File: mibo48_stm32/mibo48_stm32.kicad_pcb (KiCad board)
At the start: 2 copper layers, 55.9 x 20.3 mm, 33 parts, among them J1 Conn_01x02, J2 Conn_01x22, J3 Conn_01x22, J4 USB_B_Micro, J5 Conn_01x04, SW1 Reset, U1 STM32F303CBTx, U2 AMS1117-3.3, Y1 8MHz, Y2 32.768kHz

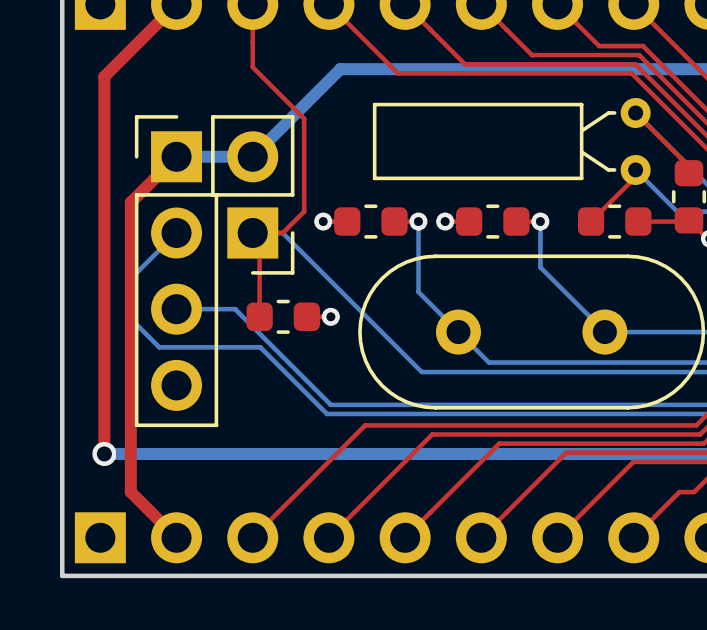
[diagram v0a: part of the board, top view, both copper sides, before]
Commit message: small layout change
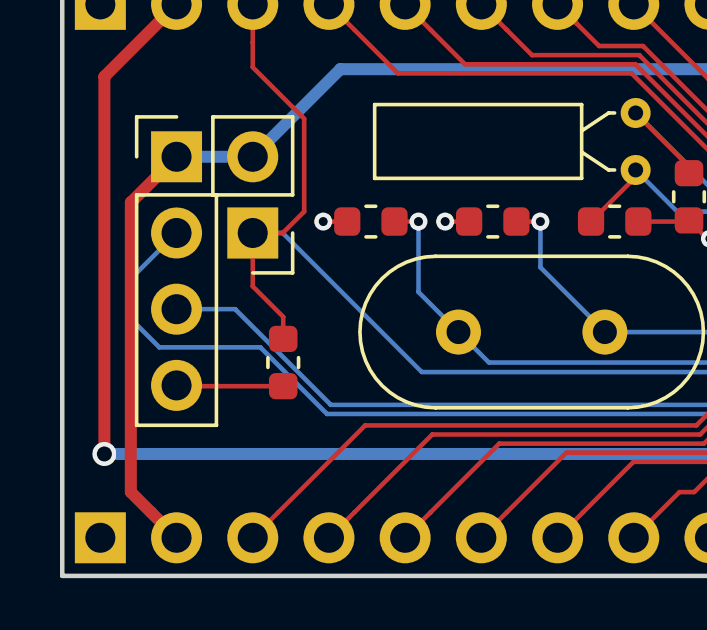
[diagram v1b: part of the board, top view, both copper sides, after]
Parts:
- moved R1 1.52 mm to (135.6, 108.5), turned to 270 degrees
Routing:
- net GND: track 33.7 -> 36.4 mm, vias 15 -> 14
- net /BOOT0: track 43.0 -> 44.0 mm
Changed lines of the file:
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@@
     (thickness 1.6)
     (drawings 7)
-    (tracks 474)
+    (tracks 475)
     (zones 0)
     (modules 33)
@@
     (45 Margin user)
     (46 B.CrtYd user hide)
-    (47 F.CrtYd user hide)
+    (47 F.CrtYd user)
     (48 B.Fab user)
     (49 F.Fab user hide)
@@
     (add_net /5V)
   )
+  (module Resistor_SMD:R_0603_1608Metric (layer F.Cu)
+    (at 135.636 108.458 270)
+    (descr "Resistor SMD 0603 (1608 Metric), square (rectangular) end terminal, IPC_7351 nominal, (Body size source: http://www.tortai-tech.com/upload/download/2011102023233369053.pdf), generated with kicad-footprint-generator")
+    (tags resistor)
+    (attr smd)
+    (fp_text reference R1 (at 0 -1.43 270) (layer F.SilkS) hide
+      (effects (font (size 1 1) (thickness 0.15)))
+    )
+    (fp_text value 100k (at 0 1.43 270) (layer F.Fab)
+      (effects (font (size 1 1) (thickness 0.15)))
+    )
+    (fp_line (start -0.8 0.4) (end -0.8 -0.4) (layer F.Fab) (width 0.1))
+    (fp_line (start -0.8 -0.4) (end 0.8 -0.4) (layer F.Fab) (width 0.1))
+    (fp_line (start 0.8 -0.4) (end 0.8 0.4) (layer F.Fab) (width 0.1))
+    (fp_line (start 0.8 0.4) (end -0.8 0.4) (layer F.Fab) (width 0.1))
+    (fp_line (start -0.162779 -0.51) (end 0.162779 -0.51) (layer F.SilkS) (width 0.12))
+    (fp_line (start -0.162779 0.51) (end 0.162779 0.51) (layer F.SilkS) (width 0.12))
+    (fp_line (start -1.48 0.73) (end -1.48 -0.73) (layer F.CrtYd) (width 0.05))
+    (fp_line (start -1.48 -0.73) (end 1.48 -0.73) (layer F.CrtYd) (width 0.05))
+    (fp_line (start 1.48 -0.73) (end 1.48 0.73) (layer F.CrtYd) (width 0.05))
+    (fp_line (start 1.48 0.73) (end -1.48 0.73) (layer F.CrtYd) (width 0.05))
+    (fp_text user %R (at 0 0 270) (layer F.Fab)
+      (effects (font (size 0.4 0.4) (thickness 0.06)))
+    )
+    (pad 1 smd roundrect (at -0.7875 0 270) (size 0.875 0.95) (layers F.Cu F.Paste F.Mask) (roundrect_rratio 0.25)
+      (net 8 /BOOT0))
+    (pad 2 smd roundrect (at 0.7875 0 270) (size 0.875 0.95) (layers F.Cu F.Paste F.Mask) (roundrect_rratio 0.25)
+      (net 1 GND))
+    (model ${KISYS3DMOD}/Resistor_SMD.3dshapes/R_0603_1608Metric.wrl
+      (at (xyz 0 0 0))
+      (scale (xyz 1 1 1))
+      (rotate (xyz 0 0 0))
+    )
+  )
   (module Button_Switch_SMD:SW_SPST_CK_RS282G05A3 (layer F.Cu)
     (at 172.974 101.219)
@@
       (net 1 GND))
     (model ${KISYS3DMOD}/Connector_PinHeader_2.54mm.3dshapes/PinHeader_1x04_P2.54mm_Vertical.wrl
-      (at (xyz 0 0 0))
-      (scale (xyz 1 1 1))
-      (rotate (xyz 0 0 0))
-    )
-  )
-  (module Resistor_SMD:R_0603_1608Metric (layer F.Cu)
-    (at 135.636 106.934)
-    (descr "Resistor SMD 0603 (1608 Metric), square (rectangular) end terminal, IPC_7351 nominal, (Body size source: http://www.tortai-tech.com/upload/download/2011102023233369053.pdf), generated with kicad-footprint-generator")
-    (tags resistor)
-    (attr smd)
-    (fp_text reference R1 (at 0 -1.43) (layer F.SilkS) hide
-      (effects (font (size 1 1) (thickness 0.15)))
-    )
-    (fp_text value 100k (at 0 1.43) (layer F.Fab)
-      (effects (font (size 1 1) (thickness 0.15)))
-    )
-    (fp_line (start -0.8 0.4) (end -0.8 -0.4) (layer F.Fab) (width 0.1))
-    (fp_line (start -0.8 -0.4) (end 0.8 -0.4) (layer F.Fab) (width 0.1))
-    (fp_line (start 0.8 -0.4) (end 0.8 0.4) (layer F.Fab) (width 0.1))
-    (fp_line (start 0.8 0.4) (end -0.8 0.4) (layer F.Fab) (width 0.1))
-    (fp_line (start -0.162779 -0.51) (end 0.162779 -0.51) (layer F.SilkS) (width 0.12))
-    (fp_line (start -0.162779 0.51) (end 0.162779 0.51) (layer F.SilkS) (width 0.12))
-    (fp_line (start -1.48 0.73) (end -1.48 -0.73) (layer F.CrtYd) (width 0.05))
-    (fp_line (start -1.48 -0.73) (end 1.48 -0.73) (layer F.CrtYd) (width 0.05))
-    (fp_line (start 1.48 -0.73) (end 1.48 0.73) (layer F.CrtYd) (width 0.05))
-    (fp_line (start 1.48 0.73) (end -1.48 0.73) (layer F.CrtYd) (width 0.05))
-    (fp_text user %R (at 0 0) (layer F.Fab)
-      (effects (font (size 0.4 0.4) (thickness 0.06)))
-    )
-    (pad 1 smd roundrect (at -0.7875 0) (size 0.875 0.95) (layers F.Cu F.Paste F.Mask) (roundrect_rratio 0.25)
-      (net 8 /BOOT0))
-    (pad 2 smd roundrect (at 0.7875 0) (size 0.875 0.95) (layers F.Cu F.Paste F.Mask) (roundrect_rratio 0.25)
-      (net 1 GND))
-    (model ${KISYS3DMOD}/Resistor_SMD.3dshapes/R_0603_1608Metric.wrl
       (at (xyz 0 0 0))
       (scale (xyz 1 1 1))
@@
   (via (at 136.9695 103.759) (size 0.6) (drill 0.3) (layers F.Cu B.Cu) (net 1))
   (segment (start 137.7695 103.759) (end 136.9695 103.759) (width 0.152) (layer F.Cu) (net 1))
-  (via (at 137.2235 106.934) (size 0.6) (drill 0.3) (layers F.Cu B.Cu) (net 1))
-  (segment (start 136.4235 106.934) (end 137.2235 106.934) (width 0.152) (layer F.Cu) (net 1))
   (segment (start 153.725112 110.917388) (end 153.2635 111.379) (width 0.152) (layer F.Cu) (net 1))
   (segment (start 154.236686 110.675994) (end 154.236125 110.676555) (width 0.152) (layer F.Cu) (net 1))
@@
   (segment (start 154.755435 103.492096) (end 154.755435 103.761538) (width 0.152) (layer F.Cu) (net 1))
   (segment (start 154.127755 102.864416) (end 154.755435 103.492096) (width 0.152) (layer F.Cu) (net 1))
+  (segment (start 132.1055 109.2455) (end 132.08 109.22) (width 0.152) (layer F.Cu) (net 1))
+  (segment (start 135.636 109.2455) (end 132.1055 109.2455) (width 0.152) (layer F.Cu) (net 1))
   (via (at 140.1445 103.759) (size 0.6) (drill 0.3) (layers F.Cu B.Cu) (net 2))
   (segment (start 139.3445 103.759) (end 140.1445 103.759) (width 0.152) (layer F.Cu) (net 2))
@@
   (segment (start 172.314 107.95) (end 171.7675 107.95) (width 0.4) (layer F.Cu) (net 5))
   (segment (start 171.7675 107.95) (end 169.291 105.4735) (width 0.4) (layer F.Cu) (net 5))
-  (via (at 159.7025 98.933) (size 0.6) (drill 0.3) (layers F.Cu B.Cu) (net 5) (status 1000000))
-  (segment (start 160.5025 99.314) (end 160.040888 98.852388) (width 0.4) (layer F.Cu) (net 5) (status 1000000))
-  (segment (start 159.783112 98.852388) (end 159.7025 98.933) (width 0.4) (layer F.Cu) (net 5) (status 1000000))
-  (segment (start 160.040888 98.852388) (end 159.783112 98.852388) (width 0.4) (layer F.Cu) (net 5) (status 1000000))
+  (via (at 159.7025 98.933) (size 0.6) (drill 0.3) (layers F.Cu B.Cu) (net 5))
+  (segment (start 160.5025 99.314) (end 160.040888 98.852388) (width 0.4) (layer F.Cu) (net 5))
+  (segment (start 159.783112 98.852388) (end 159.7025 98.933) (width 0.4) (layer F.Cu) (net 5))
+  (segment (start 160.040888 98.852388) (end 159.783112 98.852388) (width 0.4) (layer F.Cu) (net 5))
   (via (at 165.735 104.0765) (size 0.6) (drill 0.3) (layers F.Cu B.Cu) (net 5))
   (segment (start 165.7095 103.251) (end 165.7095 104.051) (width 0.4) (layer F.Cu) (net 5))
@@
   (segment (start 134.62 104.14) (end 135.622 104.14) (width 0.152) (layer F.Cu) (net 8))
   (segment (start 135.622 104.14) (end 136.3345 103.4275) (width 0.152) (layer F.Cu) (net 8))
-  (segment (start 134.8485 104.3685) (end 134.62 104.14) (width 0.152) (layer F.Cu) (net 8))
-  (segment (start 134.8485 106.934) (end 134.8485 104.3685) (width 0.152) (layer F.Cu) (net 8))
   (segment (start 135.622 104.14) (end 134.62 104.14) (width 0.152) (layer B.Cu) (net 8))
   (segment (start 140.2575 108.7755) (end 135.622 104.14) (width 0.152) (layer B.Cu) (net 8))
   (segment (start 159.1945 102.87) (end 153.289 108.7755) (width 0.152) (layer B.Cu) (net 8))
   (segment (start 153.289 108.7755) (end 140.2575 108.7755) (width 0.152) (layer B.Cu) (net 8))
+  (segment (start 135.636 107.6705) (end 135.636 106.934) (width 0.152) (layer F.Cu) (net 8))
+  (segment (start 134.62 105.918) (end 134.62 104.14) (width 0.152) (layer F.Cu) (net 8))
+  (segment (start 135.636 106.934) (end 134.62 105.918) (width 0.152) (layer F.Cu) (net 8))
   (segment (start 145.629999 113.450001) (end 144.78 114.3) (width 0.152) (layer F.Cu) (net 9))
   (segment (start 147.310456 111.769544) (end 145.629999 113.450001) (width 0.152) (layer F.Cu) (net 9))

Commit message: MIBO48 Labelling finished
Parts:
- moved R1 1.54 mm to (135.9, 106.9), turned to 0 degrees
- moved Y1 1.02 mm to (142.5, 107.4)
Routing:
- net GND: track 36.4 -> 33.7 mm, vias 14 -> 15
- net /BOOT0: track 44.0 -> 43.1 mm
- net /OSC_OUT: track 18.8 -> 18.2 mm
- net /OSC_IN: track 25.2 -> 24.7 mm
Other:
- board text added: "3.3"
- board text added: "5V"
- board text added: "A0"
- board text added: "A1"
- board text added: "A10"
- board text added: "A11"
- board text added: "A12"
- board text added: "A15"
- board text added: "A2"
- board text added: "A3"
- board text added: "A4"
- board text added: "A5"
- board text added: "A6"
- board text added: "A7"
- board text added: "A8"
- board text added: "A9"
- board text added: "B0"
- board text added: "B1"
- board text added: "B10"
- board text added: "B11"
- board text added: "B12"
- board text added: "B13"
- board text added: "B14"
- board text added: "B15"
- board text added: "B2"
- board text added: "B3"
- board text added: "B4"
- board text added: "B5"
- board text added: "B6"
- board text added: "B7"
- board text added: "B8"
- board text added: "B9"
- board text added: "C13"
- board text added: "C14"
- board text added: "C15"
- board text added: "CLK"
- board text added: "IO"
- board text added: "MIBO48"
- board text added: "MIBO48-STM32"
- board text added: "ROM BL."
- board text added: "RST"
- board text added: "STM32"
- board text added: "SWD"
- board text added: "VBAT"
- board text added: "boot0"
- board text added: "by nvitya"
